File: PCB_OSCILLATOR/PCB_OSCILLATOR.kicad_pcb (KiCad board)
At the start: 2 copper layers, 94.4 x 37.1 mm, 96 parts, among them J1 Jumper, J10 Jumper, J11 Jumper, J12 Jumper, J13 Jumper, J14 Jumper, J15 Jumper, J16 Jumper, J2 Jumper, J3 Jumper, J4 Jumper, J5 Jumper, J6 Jumper, J7 Jumper, J8 Jumper, J9 Jumper, P1 CONN_01X04, P2 MCLK_EXTERNAL, P3 SPI_AD5270_1, P4 SPI_AD5270_2, P5 SPI_AD9833_1, P6 SPI_AD9833_2, P7 CONN_01X04, U1 AD5270, U10 ADR291, U2 AD8421, U3 AD9833, U4 AD5270, U5 AD8421, U6 AD9833, U7 ADG819, U8 ADP3303, U9 AD8651

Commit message: PCB VERSION 1
Versión para imprimir de pcb
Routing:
- net /-12V: track 88.5 -> 99.1 mm, vias 0 -> 2
- net /GND: vias 66 -> 45
- net (no net): vias 0 -> 12
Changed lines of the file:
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@@
   (general
     (links 188)
-    (no_connects 1)
+    (no_connects 0)
     (area 62.454999 65.874999 157.025001 103.145001)
     (thickness 1.6)
     (drawings 6)
-    (tracks 710)
+    (tracks 715)
     (zones 0)
     (modules 96)
@@
   )
   (setup
-    (last_trace_width 0.55)
+    (last_trace_width 2)
     (user_trace_width 0.3)
     (user_trace_width 0.35)
@@
   (gr_line (start 156.75 65.95) (end 156.95 65.95) (angle 90) (layer Edge.Cuts) (width 0.15))
   (gr_line (start 62.63 65.95) (end 156.75 65.95) (angle 90) (layer Edge.Cuts) (width 0.15))
-  (via (at 81.22 69.21) (size 0.6) (drill 0.4) (layers F.Cu B.Cu) (net 1))
-  (via (at 74.7 69.33) (size 0.6) (drill 0.4) (layers F.Cu B.Cu) (net 1))
-  (via (at 78.17 70) (size 0.6) (drill 0.4) (layers F.Cu B.Cu) (net 1))
-  (via (at 78.94 71.53) (size 0.6) (drill 0.4) (layers F.Cu B.Cu) (net 1))
-  (via (at 77.18 71.55) (size 0.6) (drill 0.4) (layers F.Cu B.Cu) (net 1))
-  (via (at 78.11 72.87) (size 0.6) (drill 0.4) (layers F.Cu B.Cu) (net 1))
-  (via (at 78.94 74.19) (size 0.6) (drill 0.4) (layers F.Cu B.Cu) (net 1))
-  (via (at 77.2 74.19) (size 0.6) (drill 0.4) (layers F.Cu B.Cu) (net 1))
-  (via (at 67.48 67.12) (size 0.6) (drill 0.4) (layers F.Cu B.Cu) (net 1))
-  (via (at 68.44 68.4) (size 0.6) (drill 0.4) (layers F.Cu B.Cu) (net 1))
-  (via (at 70.73 68.25) (size 0.6) (drill 0.4) (layers F.Cu B.Cu) (net 1))
-  (via (at 73.33 68.28) (size 0.6) (drill 0.4) (layers F.Cu B.Cu) (net 1))
-  (via (at 75.94 68.28) (size 0.6) (drill 0.4) (layers F.Cu B.Cu) (net 1))
-  (via (at 78.01 68.41) (size 0.6) (drill 0.4) (layers F.Cu B.Cu) (net 1))
-  (via (at 80.03 68.4) (size 0.6) (drill 0.4) (layers F.Cu B.Cu) (net 1))
-  (via (at 81 67.24) (size 0.6) (drill 0.4) (layers F.Cu B.Cu) (net 1))
-  (via (at 79.02 67.22) (size 0.6) (drill 0.4) (layers F.Cu B.Cu) (net 1))
-  (via (at 77.08 67.22) (size 0.6) (drill 0.4) (layers F.Cu B.Cu) (net 1))
-  (via (at 71.99 67.16) (size 0.6) (drill 0.4) (layers F.Cu B.Cu) (net 1))
-  (via (at 74.75 67.15) (size 0.6) (drill 0.4) (layers F.Cu B.Cu) (net 1))
-  (via (at 69.58 67.04) (size 0.6) (drill 0.4) (layers F.Cu B.Cu) (net 1))
+  (via (at 81.22 69.21) (size 0.6) (drill 0.4) (layers F.Cu B.Cu) (net 0))
+  (via (at 79.15 70.55) (size 0.6) (drill 0.4) (layers F.Cu B.Cu) (net 0))
+  (via (at 77.48 70.49) (size 0.6) (drill 0.4) (layers F.Cu B.Cu) (net 0))
+  (via (at 79.09 74.09) (size 0.6) (drill 0.4) (layers F.Cu B.Cu) (net 0))
+  (via (at 77.52 74.11) (size 0.6) (drill 0.4) (layers F.Cu B.Cu) (net 0))
+  (via (at 67.48 67.12) (size 0.6) (drill 0.4) (layers F.Cu B.Cu) (net 0))
+  (via (at 69.71 68.37) (size 0.6) (drill 0.4) (layers F.Cu B.Cu) (net 0))
+  (via (at 74.94 68.56) (size 0.6) (drill 0.4) (layers F.Cu B.Cu) (net 0))
+  (via (at 78.01 68.41) (size 0.6) (drill 0.4) (layers F.Cu B.Cu) (net 0))
+  (via (at 81 67.24) (size 0.6) (drill 0.4) (layers F.Cu B.Cu) (net 0))
+  (via (at 77.08 67.22) (size 0.6) (drill 0.4) (layers F.Cu B.Cu) (net 0))
+  (via (at 71.99 67.16) (size 0.6) (drill 0.4) (layers F.Cu B.Cu) (net 0))
   (segment (start 142.98 71.14) (end 144.52 71.14) (width 1) (layer F.Cu) (net 1))
   (via (at 144.86 70.8) (size 0.8) (drill 0.5) (layers F.Cu B.Cu) (net 1))
@@
   (segment (start 135.25 91.865) (end 137.915 91.865) (width 0.3) (layer F.Cu) (net 44))
   (segment (start 137.915 91.865) (end 139.42 90.36) (width 0.3) (layer F.Cu) (net 44))
+  (via (at 127.195 95.965) (size 1) (drill 0.8) (layers F.Cu B.Cu) (net 45))
+  (segment (start 127.19 95.93) (end 127.19 95.96) (width 2) (layer B.Cu) (net 45))
+  (segment (start 127.19 95.96) (end 127.195 95.965) (width 2) (layer B.Cu) (net 45))
+  (segment (start 125.56 95.93) (end 127.19 95.93) (width 2) (layer B.Cu) (net 45))
+  (segment (start 127.19 95.93) (end 127.31 95.93) (width 2) (layer B.Cu) (net 45))
+  (segment (start 127.31 95.93) (end 127.44 96.06) (width 2) (layer B.Cu) (net 45))
+  (segment (start 127.195 95.965) (end 125.595 95.965) (width 2) (layer F.Cu) (net 45))
+  (segment (start 125.595 95.965) (end 125.56 95.93) (width 2) (layer F.Cu) (net 45))
+  (via (at 125.56 95.93) (size 1) (drill 0.8) (layers F.Cu B.Cu) (net 45))
+  (segment (start 121.15 97.03) (end 121.15 99.08) (width 2) (layer B.Cu) (net 45))
+  (segment (start 122.27 95.91) (end 121.15 97.03) (width 2) (layer B.Cu) (net 45))
+  (segment (start 125.54 95.91) (end 122.27 95.91) (width 2) (layer B.Cu) (net 45))
+  (segment (start 125.56 95.93) (end 125.54 95.91) (width 2) (layer B.Cu) (net 45))
   (segment (start 128.99 97.17) (end 127.81 97.17) (width 1) (layer F.Cu) (net 45))
   (segment (start 127.81 97.17) (end 126.23 98.75) (width 1) (layer F.Cu) (net 45))
@@
   (segment (start 92.81 98.83) (end 93.56 99.58) (width 1) (layer F.Cu) (net 45))
   (segment (start 126.23 99.08) (end 126.23 96.93) (width 2) (layer F.Cu) (net 45))
+  (segment (start 126.23 96.93) (end 127.195 95.965) (width 2) (layer F.Cu) (net 45))
   (segment (start 146.66 91.45) (end 146.66 89.31) (width 2) (layer F.Cu) (net 45))
-  (segment (start 146.1 92.01) (end 146.66 91.45) (width 2) (layer F.Cu) (net 45))
-  (segment (start 142.38 92.01) (end 146.1 92.01) (width 2) (layer F.Cu) (net 45))
-  (segment (start 140.2 94.19) (end 142.38 92.01) (width 2) (layer F.Cu) (net 45))
+  (segment (start 127.195 95.965) (end 128.97 94.19) (width 2) (layer F.Cu) (net 45))
   (segment (start 128.97 94.19) (end 140.2 94.19) (width 2) (layer F.Cu) (net 45))
-  (segment (start 126.23 96.93) (end 128.97 94.19) (width 2) (layer F.Cu) (net 45))
+  (segment (start 140.2 94.19) (end 142.38 92.01) (width 2) (layer F.Cu) (net 45))
+  (segment (start 142.38 92.01) (end 146.1 92.01) (width 2) (layer F.Cu) (net 45))
+  (segment (start 146.1 92.01) (end 146.66 91.45) (width 2) (layer F.Cu) (net 45))
   (segment (start 121.15 99.08) (end 121.15 100.09) (width 2) (layer F.Cu) (net 45))
   (segment (start 121.15 100.09) (end 119.6 101.64) (width 2) (layer F.Cu) (net 45))

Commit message: //
//
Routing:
- net /GND: vias 45 -> 49
- net (no net): vias 12 -> 6
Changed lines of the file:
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@@
     (thickness 1.6)
     (drawings 6)
-    (tracks 715)
+    (tracks 713)
     (zones 0)
     (modules 96)
@@
   )
   (setup
-    (last_trace_width 2)
+    (last_trace_width 0.55)
     (user_trace_width 0.3)
     (user_trace_width 0.35)
@@
   (gr_line (start 156.75 65.95) (end 156.95 65.95) (angle 90) (layer Edge.Cuts) (width 0.15))
   (gr_line (start 62.63 65.95) (end 156.75 65.95) (angle 90) (layer Edge.Cuts) (width 0.15))
-  (via (at 81.22 69.21) (size 0.6) (drill 0.4) (layers F.Cu B.Cu) (net 0))
-  (via (at 79.15 70.55) (size 0.6) (drill 0.4) (layers F.Cu B.Cu) (net 0))
-  (via (at 77.48 70.49) (size 0.6) (drill 0.4) (layers F.Cu B.Cu) (net 0))
-  (via (at 79.09 74.09) (size 0.6) (drill 0.4) (layers F.Cu B.Cu) (net 0))
-  (via (at 77.52 74.11) (size 0.6) (drill 0.4) (layers F.Cu B.Cu) (net 0))
-  (via (at 67.48 67.12) (size 0.6) (drill 0.4) (layers F.Cu B.Cu) (net 0))
-  (via (at 69.71 68.37) (size 0.6) (drill 0.4) (layers F.Cu B.Cu) (net 0))
-  (via (at 74.94 68.56) (size 0.6) (drill 0.4) (layers F.Cu B.Cu) (net 0))
-  (via (at 78.01 68.41) (size 0.6) (drill 0.4) (layers F.Cu B.Cu) (net 0))
-  (via (at 81 67.24) (size 0.6) (drill 0.4) (layers F.Cu B.Cu) (net 0))
-  (via (at 77.08 67.22) (size 0.6) (drill 0.4) (layers F.Cu B.Cu) (net 0))
-  (via (at 71.99 67.16) (size 0.6) (drill 0.4) (layers F.Cu B.Cu) (net 0))
+  (via (at 80.6 67.03) (size 0.6) (drill 0.4) (layers F.Cu B.Cu) (net 0))
+  (via (at 80.47 68.5) (size 0.6) (drill 0.4) (layers F.Cu B.Cu) (net 0))
+  (via (at 77.11 67.74) (size 0.6) (drill 0.4) (layers F.Cu B.Cu) (net 0))
+  (via (at 73.81 68.84) (size 0.6) (drill 0.4) (layers F.Cu B.Cu) (net 0))
+  (via (at 71.81 67.31) (size 0.6) (drill 0.4) (layers F.Cu B.Cu) (net 0))
+  (via (at 69.43 68.34) (size 0.6) (drill 0.4) (layers F.Cu B.Cu) (net 0))
+  (via (at 78.98 69.98) (size 0.6) (drill 0.4) (layers F.Cu B.Cu) (net 1))
+  (via (at 77.52 72.44) (size 0.6) (drill 0.4) (layers F.Cu B.Cu) (net 1))
+  (via (at 78.31 73.96) (size 0.6) (drill 0.4) (layers F.Cu B.Cu) (net 1))
+  (via (at 67.69 67.04) (size 0.6) (drill 0.4) (layers F.Cu B.Cu) (net 1))
   (segment (start 142.98 71.14) (end 144.52 71.14) (width 1) (layer F.Cu) (net 1))
   (via (at 144.86 70.8) (size 0.8) (drill 0.5) (layers F.Cu B.Cu) (net 1))

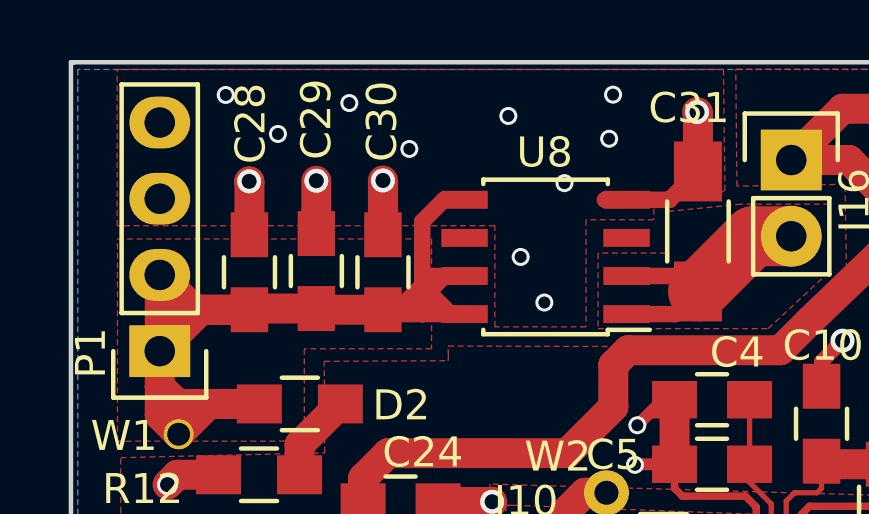
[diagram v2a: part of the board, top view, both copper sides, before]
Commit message: Cambio de regulador en esquematico
//
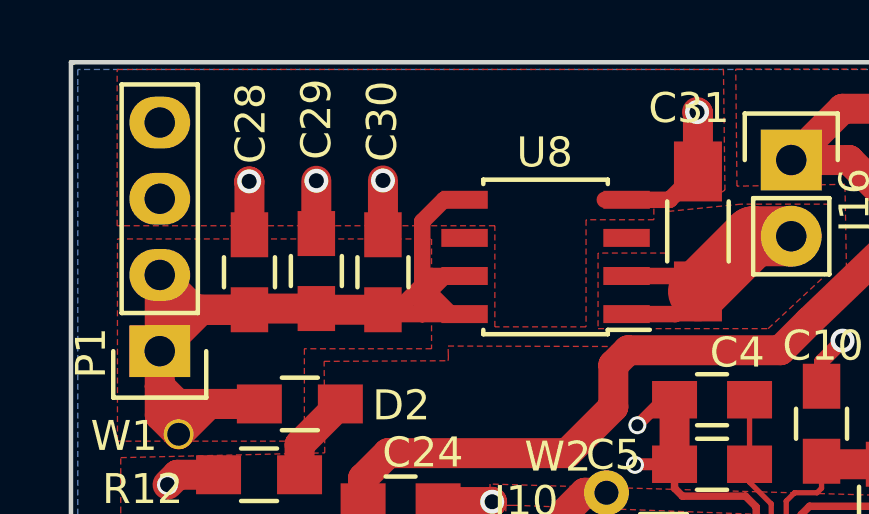
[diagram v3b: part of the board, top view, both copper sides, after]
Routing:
- net /GND: vias 49 -> 45
- net (no net): vias 6 -> 0
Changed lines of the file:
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@@
   (general
     (links 188)
-    (no_connects 0)
-    (area 62.454999 65.874999 157.025001 103.145001)
+    (no_connects 43)
+    (area 61.285 65.005 157.025001 103.145001)
     (thickness 1.6)
     (drawings 6)
-    (tracks 713)
+    (tracks 703)
     (zones 0)
     (modules 96)
@@
   )
   (setup
-    (last_trace_width 0.55)
+    (last_trace_width 0.2)
     (user_trace_width 0.3)
     (user_trace_width 0.35)
@@
   (gr_line (start 156.75 65.95) (end 156.95 65.95) (angle 90) (layer Edge.Cuts) (width 0.15))
   (gr_line (start 62.63 65.95) (end 156.75 65.95) (angle 90) (layer Edge.Cuts) (width 0.15))
-  (via (at 80.6 67.03) (size 0.6) (drill 0.4) (layers F.Cu B.Cu) (net 0))
-  (via (at 80.47 68.5) (size 0.6) (drill 0.4) (layers F.Cu B.Cu) (net 0))
-  (via (at 77.11 67.74) (size 0.6) (drill 0.4) (layers F.Cu B.Cu) (net 0))
-  (via (at 73.81 68.84) (size 0.6) (drill 0.4) (layers F.Cu B.Cu) (net 0))
-  (via (at 71.81 67.31) (size 0.6) (drill 0.4) (layers F.Cu B.Cu) (net 0))
-  (via (at 69.43 68.34) (size 0.6) (drill 0.4) (layers F.Cu B.Cu) (net 0))
-  (via (at 78.98 69.98) (size 0.6) (drill 0.4) (layers F.Cu B.Cu) (net 1))
-  (via (at 77.52 72.44) (size 0.6) (drill 0.4) (layers F.Cu B.Cu) (net 1))
-  (via (at 78.31 73.96) (size 0.6) (drill 0.4) (layers F.Cu B.Cu) (net 1))
-  (via (at 67.69 67.04) (size 0.6) (drill 0.4) (layers F.Cu B.Cu) (net 1))
   (segment (start 142.98 71.14) (end 144.52 71.14) (width 1) (layer F.Cu) (net 1))
   (via (at 144.86 70.8) (size 0.8) (drill 0.5) (layers F.Cu B.Cu) (net 1))
@@
     (connect_pads yes (clearance 0.3))
     (min_thickness 0.2)
-    (fill yes (arc_segments 16) (thermal_gap 0.508) (thermal_bridge_width 0.508) (smoothing fillet))
+    (fill (arc_segments 16) (thermal_gap 0.508) (thermal_bridge_width 0.508) (smoothing fillet))
     (polygon
       (pts
@@
     (connect_pads yes (clearance 0.3))
     (min_thickness 0.2)
-    (fill yes (arc_segments 16) (thermal_gap 0.508) (thermal_bridge_width 0.508) (smoothing fillet))
+    (fill (arc_segments 16) (thermal_gap 0.508) (thermal_bridge_width 0.508) (smoothing fillet))
     (polygon
       (pts
@@
     (connect_pads yes (clearance 0.3))
     (min_thickness 0.2)
-    (fill yes (arc_segments 16) (thermal_gap 0.508) (thermal_bridge_width 0.508) (smoothing fillet))
+    (fill (arc_segments 16) (thermal_gap 0.508) (thermal_bridge_width 0.508) (smoothing fillet))
     (polygon
       (pts
@@
     (connect_pads (clearance 0.4))
     (min_thickness 0.2)
-    (fill yes (arc_segments 16) (thermal_gap 0.508) (thermal_bridge_width 0.508) (smoothing fillet))
+    (fill (arc_segments 16) (thermal_gap 0.508) (thermal_bridge_width 0.508) (smoothing fillet))
     (polygon
       (pts
@@
     (connect_pads (clearance 0.4))
     (min_thickness 0.2)
-    (fill yes (arc_segments 16) (thermal_gap 0.508) (thermal_bridge_width 0.508) (smoothing fillet))
+    (fill (arc_segments 16) (thermal_gap 0.508) (thermal_bridge_width 0.508) (smoothing fillet))
     (polygon
       (pts
@@
     (connect_pads (clearance 0.4))
     (min_thickness 0.2)
-    (fill yes (arc_segments 16) (thermal_gap 0.508) (thermal_bridge_width 0.508))
+    (fill (arc_segments 16) (thermal_gap 0.508) (thermal_bridge_width 0.508))
     (polygon
       (pts
@@
     (connect_pads (clearance 0.4))
     (min_thickness 0.2)
-    (fill yes (arc_segments 16) (thermal_gap 0.508) (thermal_bridge_width 0.508))
+    (fill (arc_segments 16) (thermal_gap 0.508) (thermal_bridge_width 0.508))
     (polygon
       (pts
@@
     (connect_pads (clearance 0.4))
     (min_thickness 0.2)
-    (fill yes (arc_segments 16) (thermal_gap 0.508) (thermal_bridge_width 0.508))
+    (fill (arc_segments 16) (thermal_gap 0.508) (thermal_bridge_width 0.508))
     (polygon
       (pts
@@
     (connect_pads (clearance 0.4))
     (min_thickness 0.3)
-    (fill yes (arc_segments 16) (thermal_gap 0.508) (thermal_bridge_width 0.508))
+    (fill (arc_segments 16) (thermal_gap 0.508) (thermal_bridge_width 0.508))
     (polygon
       (pts

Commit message: Ultima Version
//
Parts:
- added ?: MountingHole_2.2mm_M2_Pad_Via, Mounting_Holes:MountingHole_2.2mm_M2_Pad_Via, F.Cu at (151.1, 98.6)
- added ?: MountingHole_2.2mm_M2_Pad_Via, Mounting_Holes:MountingHole_2.2mm_M2_Pad_Via, F.Cu at (68.5, 96.2)
- added ?: MountingHole_2.2mm_M2_Pad_Via, Mounting_Holes:MountingHole_2.2mm_M2_Pad_Via, F.Cu at (119.7, 69.3)
- added C33: 1uF, Capacitors_SMD:C_0805_HandSoldering, F.Cu at (77.1, 75.9)
- added R7: 140K, Resistors_SMD:R_0805_HandSoldering, F.Cu at (74.6, 67.9)
- added R8: 78.7K, Resistors_SMD:R_0805_HandSoldering, F.Cu at (79.7, 67.9)
- C31: value 0.47uF -> CNR
- U8: value ADP3303 -> ADP3334
- moved C30 0.61 mm to (73.0, 72.3)
- moved C28 0.59 mm to (68.5, 72.4)
- moved C29 0.55 mm to (70.7, 72.4)
- moved U8 0.47 mm to (78.2, 72.0), turned to 0 degrees
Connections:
- C31 pad 2: /GND -> Net-(C31-Pad2)
- U8 pad 1: Net-(C31-Pad1) -> /GND
- U8 pad 2: Net-(C31-Pad1) -> /GND
- U8 pad 3: (no net) -> /+5V
- U8 pad 4: /GND -> /+5V
- U8 pad 5: /+5V -> Net-(C31-Pad1)
- U8 pad 6: (no net) -> Net-(C31-Pad1)
- U8 pad 7: /+5V -> Net-(C31-Pad2)
- U8 pad 8: /+5V -> (no net)
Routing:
- net /GND: track 153.5 -> 215.4 mm, vias 45 -> 61
- net Net-(C31-Pad1): track 9.16 -> 23.7 mm
- net /+5V: track 39.9 -> 26.1 mm
- net Net-(C31-Pad2): track 0.00 -> 11.0 mm
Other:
- board text added: "SBS"
- board text added: "SBS Module: 001"
- board text added: "e"
- board text added: "n"
- board text added: "o"
